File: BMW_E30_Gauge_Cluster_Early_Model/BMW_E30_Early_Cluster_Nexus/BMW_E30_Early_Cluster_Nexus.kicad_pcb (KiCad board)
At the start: 2 copper layers, 356.8 x 150 mm, 27 parts, among them J1 C1 - Blue Connector, J2 C2 - White Connector, J3 C3 - Yellow Connector, J4 Conn_01x16_Pin, J5 Conn_01x19_Socket, U1 Temperature Gauge, U2 Fuel Gauge

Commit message: Move Board Cut Outline
Moved board cut outlines up by 0.3mm to more closely match the original board's fit on the plastic back shell. Final step will be to update J5 to the new design from the late model project.
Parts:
- moved J1 0.30 mm to (335.5, 164.1)
- moved J2 0.30 mm to (80.5, 164.1)
- moved J3 0.30 mm to (215.6, 206.8)
- moved JP1 0.30 mm to (229.0, 213.5)
- moved LA11 0.30 mm to (329.7, 213.3)
- moved LA12 0.30 mm to (349.8, 212.0)
- moved LA14 0.30 mm to (43.0, 174.3)
- moved LA15 0.30 mm to (208.0, 189.8)
- moved LA20 0.30 mm to (374.6, 175.3)
- moved LA4 0.30 mm to (126.9, 212.0)
- moved LA5 0.30 mm to (147.0, 212.0)
- moved LA7 0.30 mm to (249.1, 212.0)
- moved LA8 0.30 mm to (269.3, 212.0)
- moved LA9 0.30 mm to (289.5, 212.0)
- moved R1 0.30 mm to (320.3, 173.9)
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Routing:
- net +12 T15: track 904.4 -> 906.1 mm
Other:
- outline, holes or cut-outs redrawn

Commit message: Updated Connector V Footprint
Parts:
- J1: value C1 - Blue Connector -> C1 - Blue Connector (TE_827881-3)
- J2: value C2 - White Connector -> C2 - White Connector (TE_827881-2)
- J3: value C3 - Yellow Connector -> C3 - Yellow Connector (TE_827881-1)
- J4: value Conn_01x16_Pin -> EG_Tach_Spdometer
- J5: value Conn_01x19_Socket -> SI Board Interface; footprint BMW_Cluster_Connectors:ConnectorV_Early -> BMW_Cluster_Connectors:ConnectorV_Early_V2
- moved J5 32.7 mm to (240.0, 221.4)
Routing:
- net unconnected-(J5-Pin_18-Pad18): track 0.00 -> 8.54 mm
- net GNDPWR: track 861.5 -> 868.8 mm
- net Distance_pulse: track 90.5 -> 95.7 mm
- net +12 T30: track 241.2 -> 246.3 mm
- net cylinder_count: track 98.5 -> 103.6 mm
- net Speed_pulse: track 94.7 -> 99.6 mm
- net Brake_wear_sig-: track 141.6 -> 146.6 mm
- net Brake_wear_sig+: track 229.0 -> 233.9 mm
- net SI_RST: track 244.0 -> 248.8 mm
- net Eng_temp_sensor: track 284.5 -> 289.3 mm
- net Brake_wear_ind+: track 48.3 -> 52.7 mm
- net START: track 157.4 -> 161.5 mm
- net +5V: track 252.4 -> 255.6 mm
- net Temp_gauge: track 208.6 -> 210.5 mm
- net Illum+: track 319.9 -> 320.5 mm

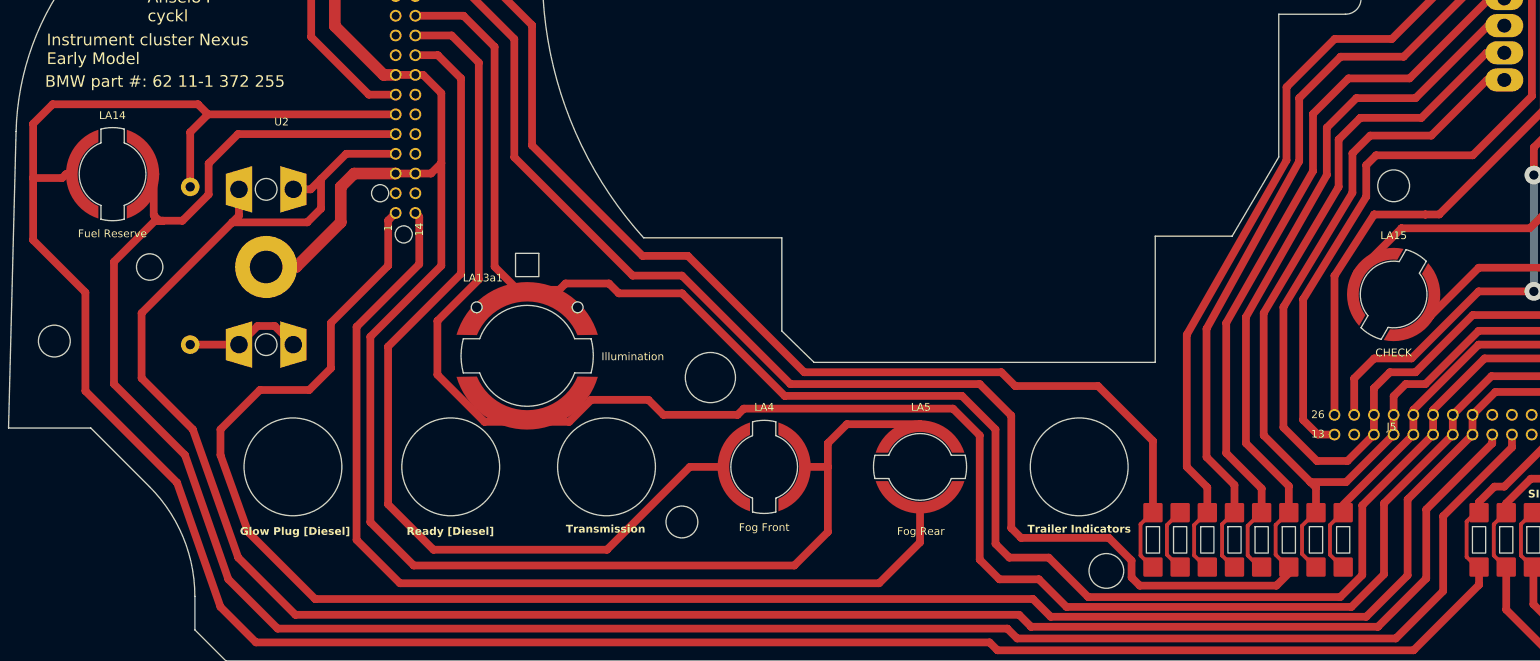
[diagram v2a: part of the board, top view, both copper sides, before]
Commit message: Update Silkscreen for Connector V
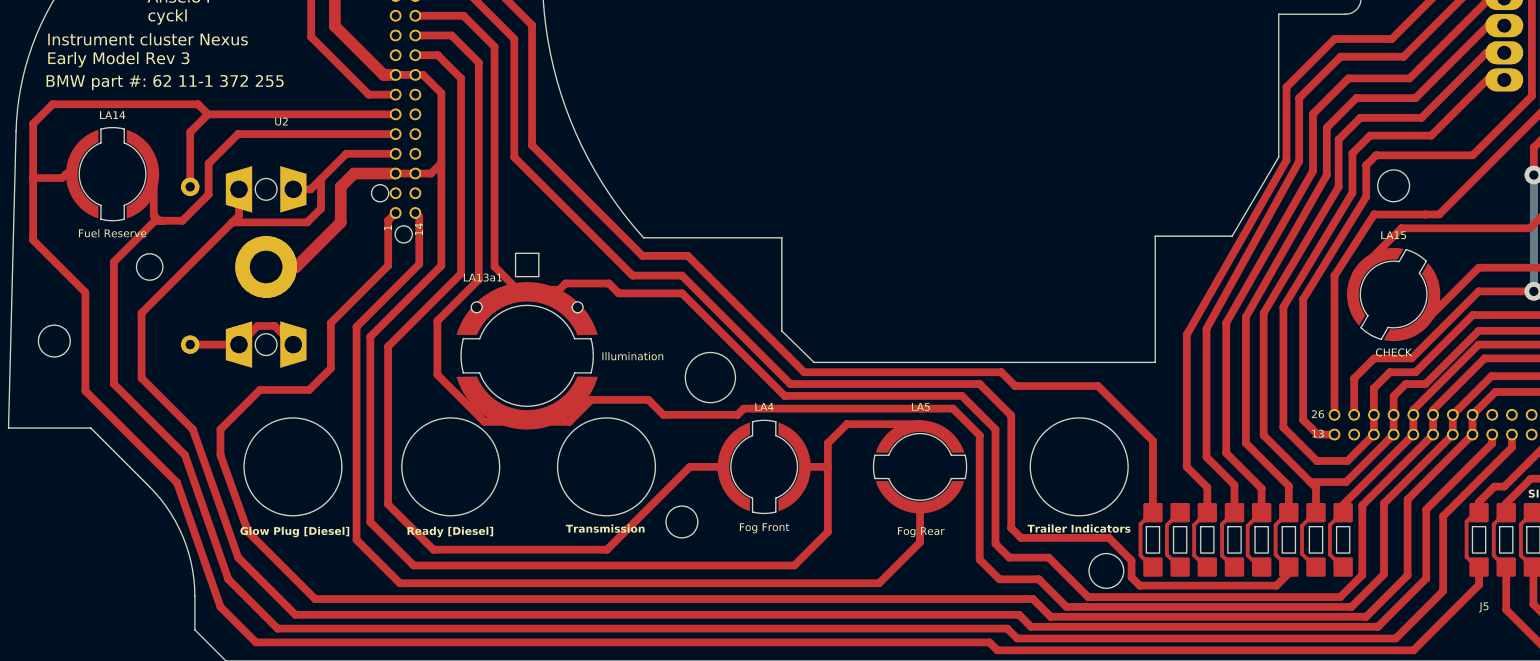
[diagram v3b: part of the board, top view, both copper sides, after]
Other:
- board text added: "Instrument cluster Nexus Early Model Rev 3"
- board text removed: "Instrument cluster Nexus Early Model"
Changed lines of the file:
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@@
 		(descr "Connector V for early model cluster, connects nexus board to SI board. ")
 		(property "Reference" "J5"
-			(at -32.269602 -14.559911 0)
+			(at -20.3 8.596 0)
 			(unlocked yes)
 			(layer "F.SilkS")
@@
 		)
 	)
-	(gr_text "Instrument cluster Nexus\nEarly Model"
+	(gr_text "Instrument cluster Nexus\nEarly Model Rev 3"
 		(at 34.5 160.3 0)
 		(layer "F.SilkS")
